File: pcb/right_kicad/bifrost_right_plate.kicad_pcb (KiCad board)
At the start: 2 copper layers, 148.4 x 87.2 mm, 27 parts

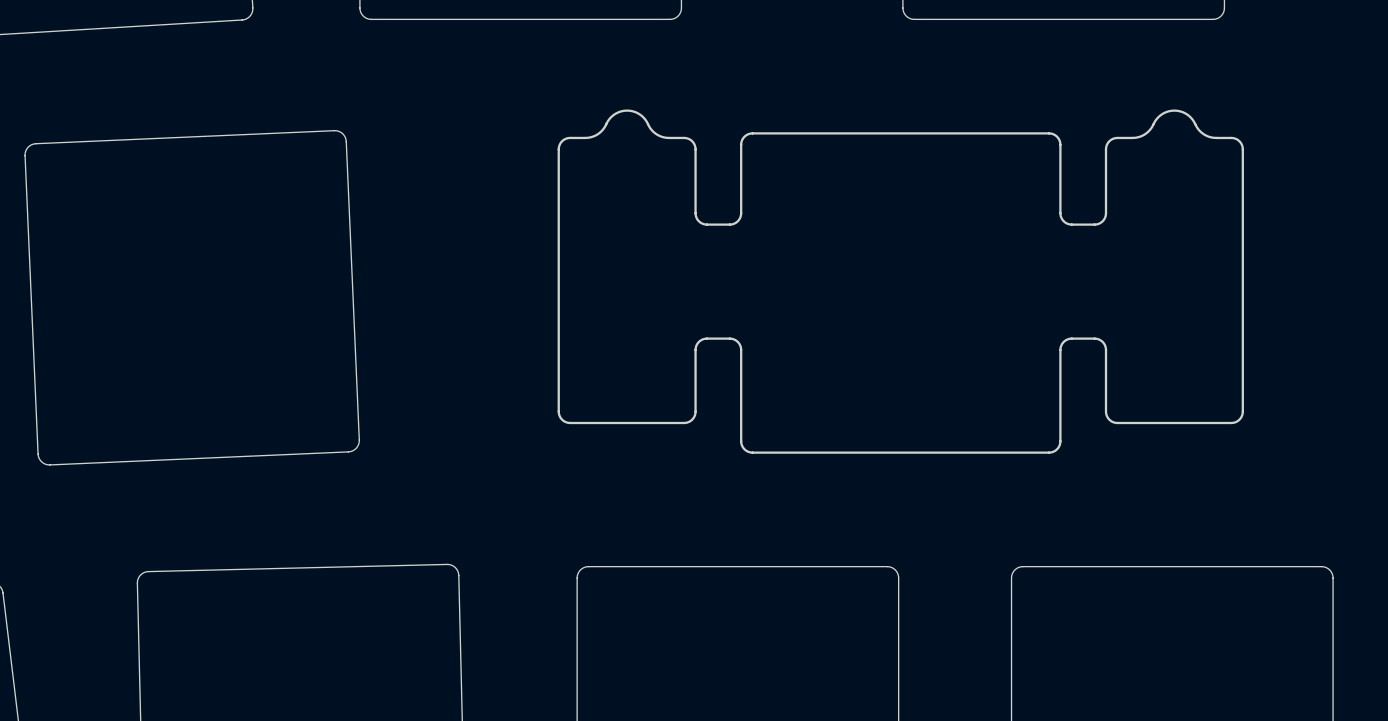
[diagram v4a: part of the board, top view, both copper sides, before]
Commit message: Update PCB plate and stabilizer designs
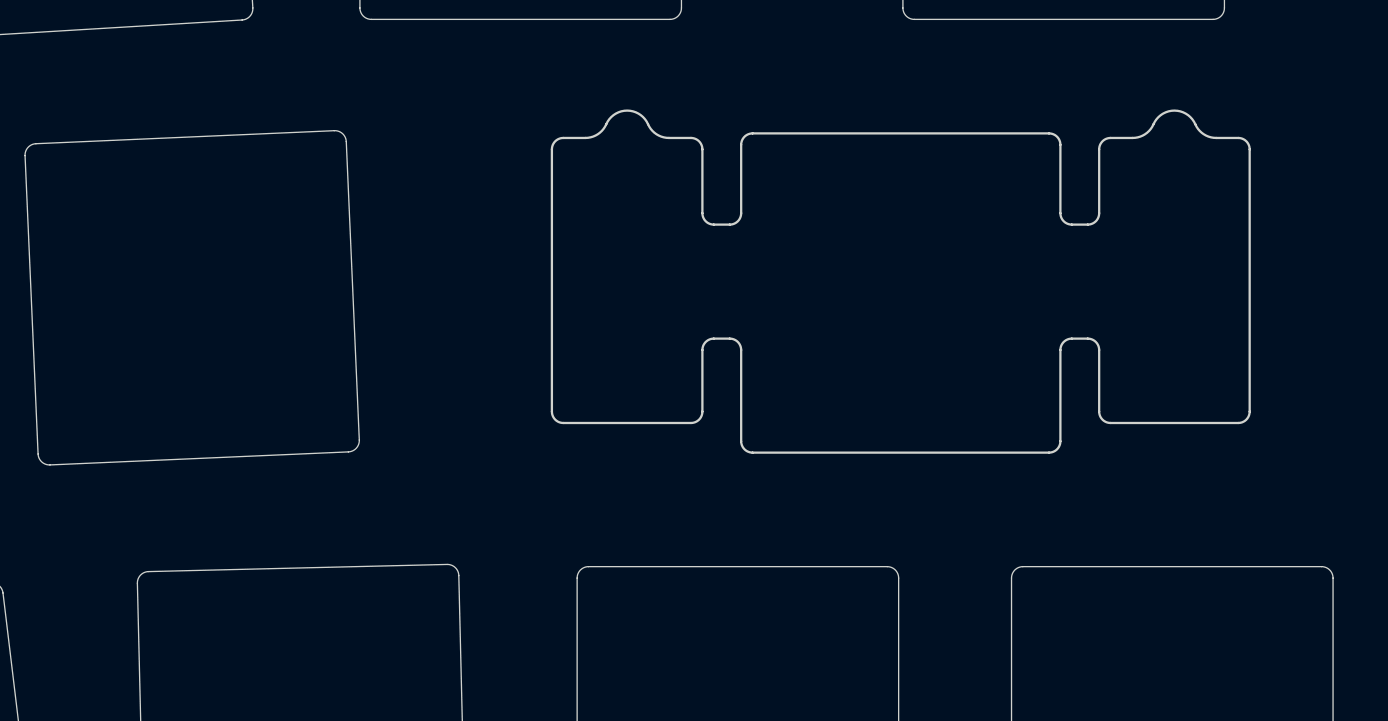
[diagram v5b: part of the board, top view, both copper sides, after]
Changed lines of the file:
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@@
 		(duplicate_pad_numbers_are_jumpers no)
 		(fp_line
-			(start -15 5.2)
-			(end -15 -6.3)
-			(stroke
-				(width 0.1)
-				(type default)
-			)
-			(layer "Edge.Cuts")
-		)
-		(fp_line
-			(start -14.5 -6.8)
+			(start -15.3 5.2)
+			(end -15.3 -6.3)
+			(stroke
+				(width 0.1)
+				(type default)
+			)
+			(layer "Edge.Cuts")
+		)
+		(fp_line
+			(start -14.8 -6.8)
 			(end -13.83303 -6.8)
 			(stroke
@@
 		(fp_line
 			(start -10.16697 -6.8)
-			(end -9.5 -6.8)
-			(stroke
-				(width 0.1)
-				(type default)
-			)
-			(layer "Edge.Cuts")
-		)
-		(fp_line
-			(start -9.5 5.7)
-			(end -14.5 5.7)
-			(stroke
-				(width 0.1)
-				(type default)
-			)
-			(layer "Edge.Cuts")
-		)
-		(fp_line
-			(start -9 -6.3)
-			(end -9 -3.5)
-			(stroke
-				(width 0.1)
-				(type default)
-			)
-			(layer "Edge.Cuts")
-		)
-		(fp_line
-			(start -9 2.5)
-			(end -9 5.2)
-			(stroke
-				(width 0.1)
-				(type default)
-			)
-			(layer "Edge.Cuts")
-		)
-		(fp_line
-			(start -8.5 -3)
+			(end -9.2 -6.8)
+			(stroke
+				(width 0.1)
+				(type default)
+			)
+			(layer "Edge.Cuts")
+		)
+		(fp_line
+			(start -9.2 5.7)
+			(end -14.8 5.7)
+			(stroke
+				(width 0.1)
+				(type default)
+			)
+			(layer "Edge.Cuts")
+		)
+		(fp_line
+			(start -8.7 -6.3)
+			(end -8.7 -3.5)
+			(stroke
+				(width 0.1)
+				(type default)
+			)
+			(layer "Edge.Cuts")
+		)
+		(fp_line
+			(start -8.7 2.5)
+			(end -8.7 5.2)
+			(stroke
+				(width 0.1)
+				(type default)
+			)
+			(layer "Edge.Cuts")
+		)
+		(fp_line
+			(start -8.2 -3)
 			(end -7.5 -3)
 			(stroke
@@
 		(fp_line
 			(start -7.5 2)
-			(end -8.5 2)
+			(end -8.2 2)
 			(stroke
 				(width 0.1)
@@
 		(fp_line
 			(start 7.5 -3)
-			(end 8.5 -3)
-			(stroke
-				(width 0.1)
-				(type default)
-			)
-			(layer "Edge.Cuts")
-		)
-		(fp_line
-			(start 8.5 2)
+			(end 8.2 -3)
+			(stroke
+				(width 0.1)
+				(type default)
+			)
+			(layer "Edge.Cuts")
+		)
+		(fp_line
+			(start 8.2 2)
 			(end 7.5 2)
 			(stroke
@@
 		)
 		(fp_line
-			(start 9 -3.5)
-			(end 9 -6.3)
-			(stroke
-				(width 0.1)
-				(type default)
-			)
-			(layer "Edge.Cuts")
-		)
-		(fp_line
-			(start 9 5.2)
-			(end 9 2.5)
-			(stroke
-				(width 0.1)
-				(type default)
-			)
-			(layer "Edge.Cuts")
-		)
-		(fp_line
-			(start 9.5 -6.8)
+			(start 8.7 -3.5)
+			(end 8.7 -6.3)
+			(stroke
+				(width 0.1)
+				(type default)
+			)
+			(layer "Edge.Cuts")
+		)
+		(fp_line
+			(start 8.7 5.2)
+			(end 8.7 2.5)
+			(stroke
+				(width 0.1)
+				(type default)
+			)
+			(layer "Edge.Cuts")
+		)
+		(fp_line
+			(start 9.2 -6.8)
 			(end 10.16697 -6.8)
 			(stroke
@@
 		(fp_line
 			(start 13.83303 -6.8)
-			(end 14.5 -6.8)
-			(stroke
-				(width 0.1)
-				(type default)
-			)
-			(layer "Edge.Cuts")
-		)
-		(fp_line
-			(start 14.5 5.7)
-			(end 9.5 5.7)
-			(stroke
-				(width 0.1)
-				(type default)
-			)
-			(layer "Edge.Cuts")
-		)
-		(fp_line
-			(start 15 -6.3)
-			(end 15 5.2)
-			(stroke
-				(width 0.1)
-				(type default)
-			)
-			(layer "Edge.Cuts")
-		)
-		(fp_arc
-			(start -15 -6.3)
-			(mid -14.853553 -6.653553)
-			(end -14.5 -6.8)
-			(stroke
-				(width 0.1)
-				(type default)
-			)
-			(layer "Edge.Cuts")
-		)
-		(fp_arc
-			(start -14.5 5.7)
-			(mid -14.853553 5.553553)
-			(end -15 5.2)
+			(end 14.8 -6.8)
+			(stroke
+				(width 0.1)
+				(type default)
+			)
+			(layer "Edge.Cuts")
+		)
+		(fp_line
+			(start 14.8 5.7)
+			(end 9.2 5.7)
+			(stroke
+				(width 0.1)
+				(type default)
+			)
+			(layer "Edge.Cuts")
+		)
+		(fp_line
+			(start 15.3 -6.3)
+			(end 15.3 5.2)
+			(stroke
+				(width 0.1)
+				(type default)
+			)
+			(layer "Edge.Cuts")
+		)
+		(fp_arc
+			(start -15.3 -6.3)
+			(mid -15.153553 -6.653553)
+			(end -14.8 -6.8)
+			(stroke
+				(width 0.1)
+				(type default)
+			)
+			(layer "Edge.Cuts")
+		)
+		(fp_arc
+			(start -14.8 5.7)
+			(mid -15.153553 5.553553)
+			(end -15.3 5.2)
 			(stroke
 				(width 0.1)
@@
 		)
 		(fp_arc
-			(start -9.5 -6.8)
-			(mid -9.146447 -6.653553)
-			(end -9 -6.3)
-			(stroke
-				(width 0.1)
-				(type default)
-			)
-			(layer "Edge.Cuts")
-		)
-		(fp_arc
-			(start -9 2.5)
-			(mid -8.853553 2.146447)
-			(end -8.5 2)
-			(stroke
-				(width 0.1)
-				(type default)
-			)
-			(layer "Edge.Cuts")
-		)
-		(fp_arc
-			(start -9 5.2)
-			(mid -9.146447 5.553553)
-			(end -9.5 5.7)
-			(stroke
-				(width 0.1)
-				(type default)
-			)
-			(layer "Edge.Cuts")
-		)
-		(fp_arc
-			(start -8.5 -3)
-			(mid -8.853553 -3.146447)
-			(end -9 -3.5)
+			(start -9.2 -6.8)
+			(mid -8.846447 -6.653553)
+			(end -8.7 -6.3)
+			(stroke
+				(width 0.1)
+				(type default)
+			)
+			(layer "Edge.Cuts")
+		)
+		(fp_arc
+			(start -8.7 2.5)
+			(mid -8.553553 2.146447)
+			(end -8.2 2)
+			(stroke
+				(width 0.1)
+				(type default)
+			)
+			(layer "Edge.Cuts")
+		)
+		(fp_arc
+			(start -8.7 5.2)
+			(mid -8.846447 5.553553)
+			(end -9.2 5.7)
+			(stroke
+				(width 0.1)
+				(type default)
+			)
+			(layer "Edge.Cuts")
+		)
+		(fp_arc
+			(start -8.2 -3)
+			(mid -8.553553 -3.146447)
+			(end -8.7 -3.5)
 			(stroke
 				(width 0.1)
@@
 		)
 		(fp_arc
-			(start 8.5 2)
-			(mid 8.853553 2.146447)
-			(end 9 2.5)
-			(stroke
-				(width 0.1)
-				(type default)
-			)
-			(layer "Edge.Cuts")
-		)
-		(fp_arc
-			(start 9 -6.3)
-			(mid 9.146447 -6.653553)
-			(end 9.5 -6.8)
-			(stroke
-				(width 0.1)
-				(type default)
-			)
-			(layer "Edge.Cuts")
-		)
-		(fp_arc
-			(start 9 -3.5)
-			(mid 8.853553 -3.146447)
-			(end 8.5 -3)
-			(stroke
-				(width 0.1)
-				(type default)
-			)
-			(layer "Edge.Cuts")
-		)
-		(fp_arc
-			(start 9.5 5.7)
-			(mid 9.146447 5.553553)
-			(end 9 5.2)
+			(start 8.2 2)
+			(mid 8.553553 2.146447)
+			(end 8.7 2.5)
+			(stroke
+				(width 0.1)
+				(type default)
+			)
+			(layer "Edge.Cuts")
+		)
+		(fp_arc
+			(start 8.7 -6.3)
+			(mid 8.846447 -6.653553)
+			(end 9.2 -6.8)
+			(stroke
+				(width 0.1)
+				(type default)
+			)
+			(layer "Edge.Cuts")
+		)
+		(fp_arc
+			(start 8.7 -3.5)
+			(mid 8.553553 -3.146447)
+			(end 8.2 -3)
+			(stroke
+				(width 0.1)
+				(type default)
+			)
+			(layer "Edge.Cuts")
+		)
+		(fp_arc
+			(start 9.2 5.7)
+			(mid 8.846447 5.553553)
+			(end 8.7 5.2)
 			(stroke
 				(width 0.1)
@@
 		)
 		(fp_arc
-			(start 14.5 -6.8)
-			(mid 14.853553 -6.653553)
-			(end 15 -6.3)
-			(stroke
-				(width 0.1)
-				(type default)
-			)
-			(layer "Edge.Cuts")
-		)
-		(fp_arc
-			(start 15 5.2)
-			(mid 14.853553 5.553553)
-			(end 14.5 5.7)
+			(start 14.8 -6.8)
+			(mid 15.153553 -6.653553)
+			(end 15.3 -6.3)
+			(stroke
+				(width 0.1)
+				(type default)
+			)
+			(layer "Edge.Cuts")
+		)
+		(fp_arc
+			(start 15.3 5.2)
+			(mid 15.153553 5.553553)
+			(end 14.8 5.7)
 			(stroke
 				(width 0.1)
@@
 		)
 		(fp_line
-			(start -6.55 -7.050003)
+			(start -6.55 -7.050005)
 			(end 6.55 -7.05)
 			(stroke
@@
 		)
 		(fp_line
-			(start 6.55 7.050003)
+			(start 6.55 7.050005)
 			(end -6.55 7.05)
 			(stroke
@@
 		)
 		(fp_line
-			(start 7.050003 -6.55)
+			(start 7.050005 -6.55)
 			(end 7.05 6.55)
 			(stroke
@@
 			(start -7.05 -6.55)
 			(mid -6.903553 -6.903553)
-			(end -6.55 -7.050003)
+			(end -6.55 -7.050005)
 			(stroke
 				(width 0.05)
@@
 		(fp_arc
 			(start -7.05 -6.55)
-			(mid -6.903556 -6.903553)
+			(mid -6.903558 -6.903553)
 			(end -6.55 -7.05)
 			(stroke
